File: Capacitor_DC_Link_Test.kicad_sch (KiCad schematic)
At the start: 10 parts, among them J1 Conn_01x02, J2 Conn_01x02, J3 Conn_01x02, J4 Conn_01x02, J5 Conn_01x02, J6 Conn_01x02

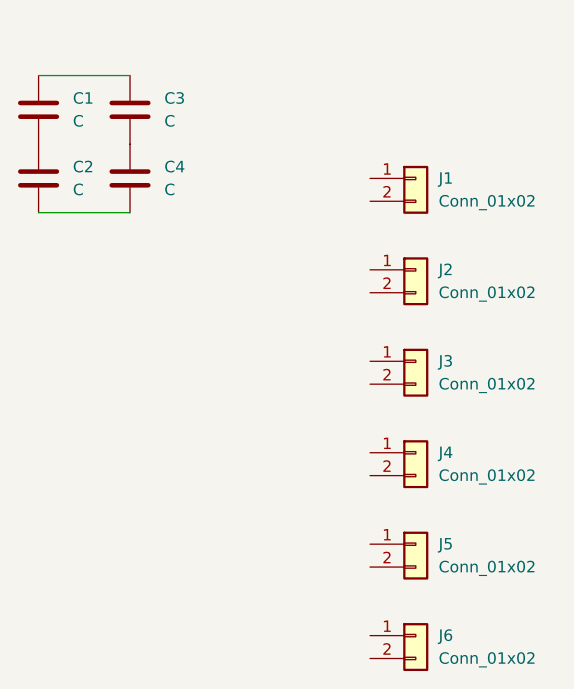
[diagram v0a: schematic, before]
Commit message: VER1.0: добавил модели конденсаторов
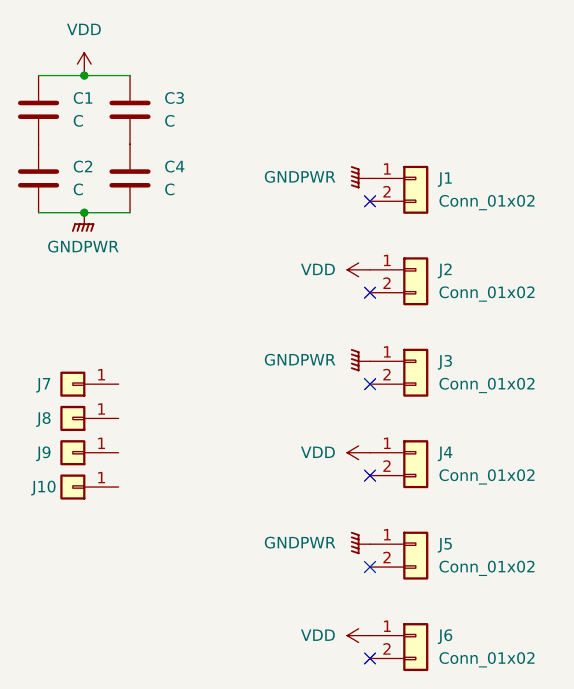
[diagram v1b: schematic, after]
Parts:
- added J10, J7, J8, J9: Conn_01x01, Bush_my:Bush_5x3, symbol Connector_Generic:Conn_01x01
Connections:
- net VDD: now reaches C1.1, C3.1
- net VDD: now also J2.1 (Pin_1), J4.1 (Pin_1), J6.1 (Pin_1)
- net GNDPWR: now reaches J1.1 (Pin_1)
- net GNDPWR: now also C2.2, C4.2, J3.1 (Pin_1), J5.1 (Pin_1)
- no-connect marks 0 -> 6

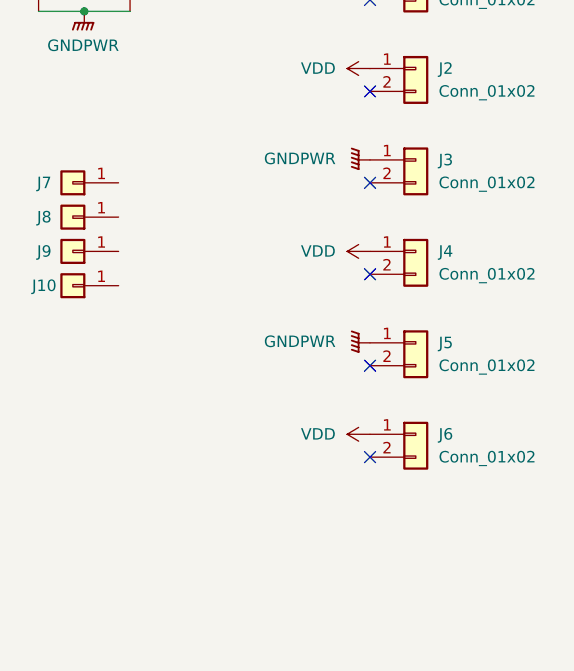
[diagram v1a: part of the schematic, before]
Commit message: VER1.0: расширил плату
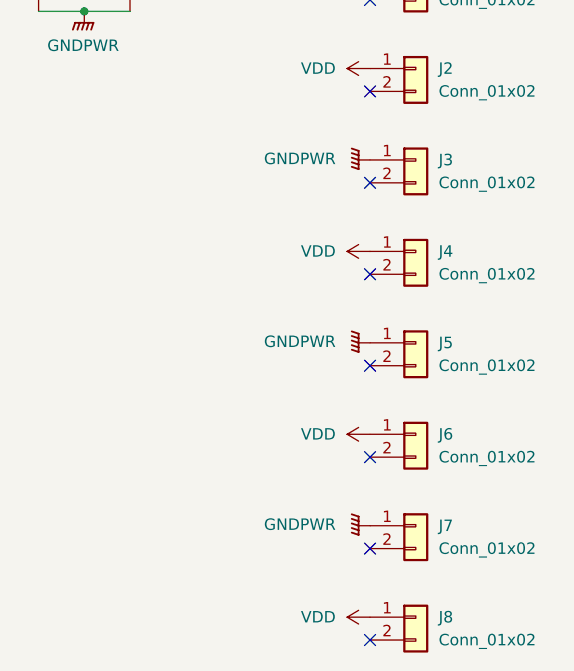
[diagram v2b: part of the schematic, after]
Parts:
- removed J10, J7, J8, J9: Conn_01x01, Bush_my:Bush_5x3, symbol Connector_Generic:Conn_01x01
- added J7: Conn_01x02, Bush_My:Low_IN, symbol Connector_Generic:Conn_01x02
- added J8: Conn_01x02, Bush_My:High_IN, symbol Connector_Generic:Conn_01x02
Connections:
- net GNDPWR: now also J7.1 (Pin_1)
- net VDD: now also J8.1 (Pin_1)
- no-connect marks 6 -> 8

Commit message: VER1.0: добавил вводные шины
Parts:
- added J10, J11, J12, J9: Conn_01x01, Bush_My:Bush_5x3, symbol Connector_Generic:Conn_01x01
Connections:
- net GNDPWR: now also J10.1 (Pin_1), J12.1 (Pin_1)
- net VDD: now also J11.1 (Pin_1), J9.1 (Pin_1)

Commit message: VER1.0: изменил шины
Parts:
- added J13, J14, J15, J16: Conn_01x01, Bush_My:Bush_5x3, symbol Connector_Generic:Conn_01x01
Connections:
- net GNDPWR: now also J14.1 (Pin_1), J16.1 (Pin_1)
- net VDD: now also J13.1 (Pin_1), J15.1 (Pin_1)
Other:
- moved on the sheet: C1, C2, C3, C4, J1, J10, J11, J12, J2, J3, J4, J5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
